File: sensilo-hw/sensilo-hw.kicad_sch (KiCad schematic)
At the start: 1 part

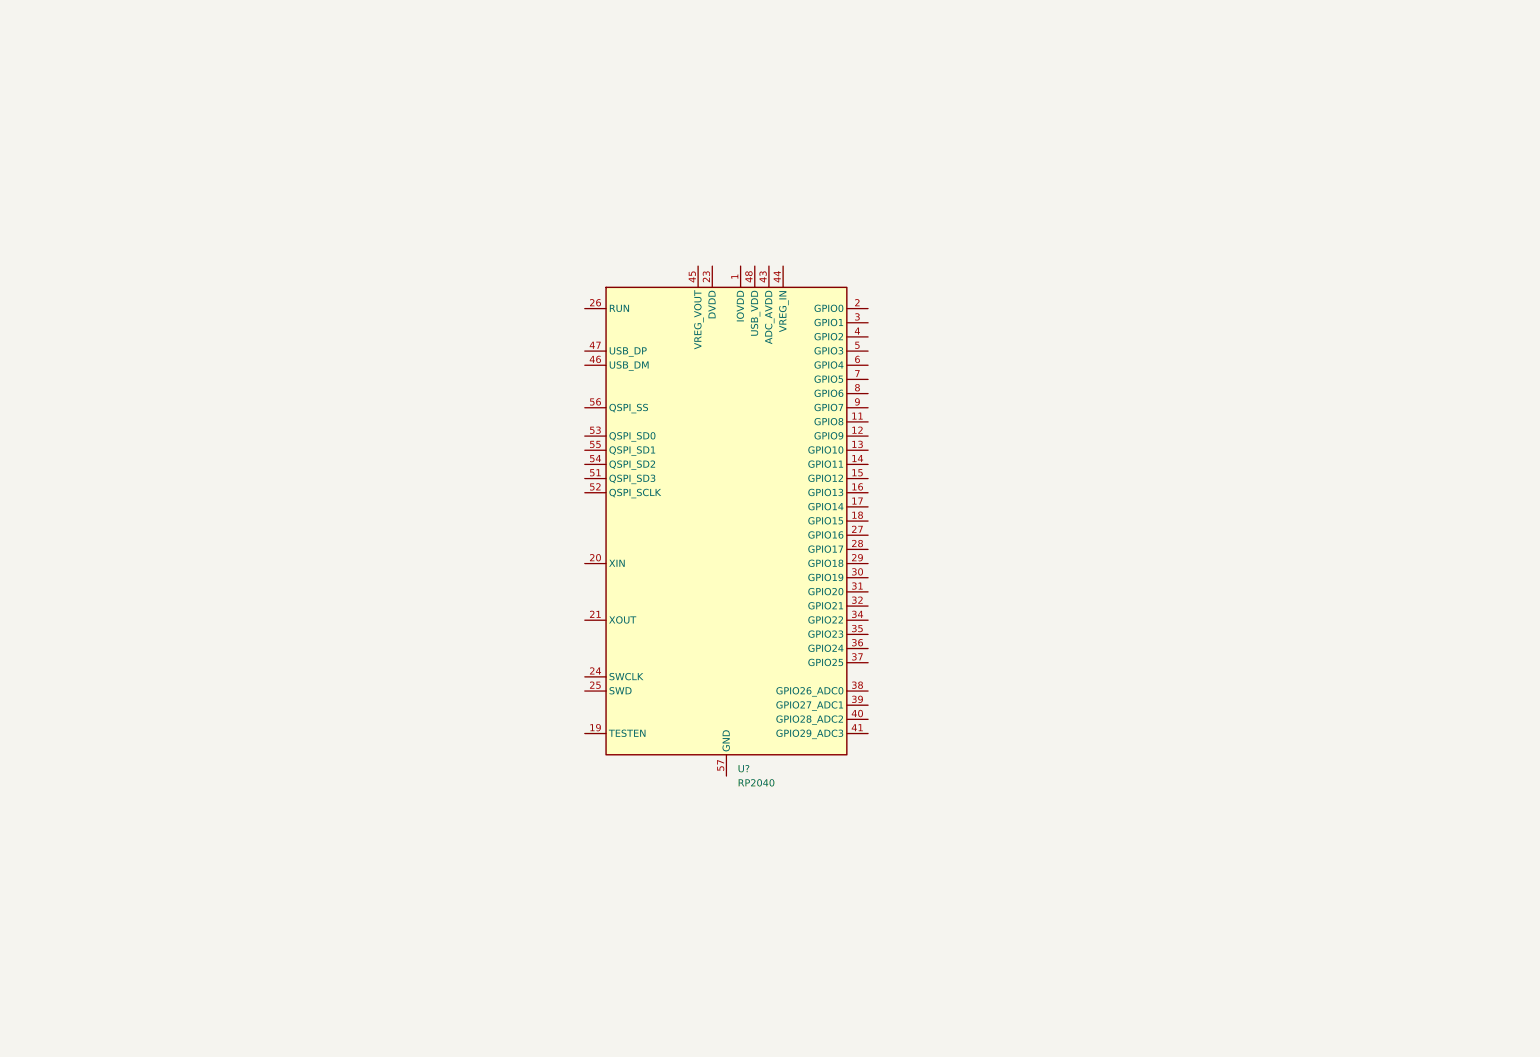
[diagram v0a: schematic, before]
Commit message: Schematic complete up to 40pc
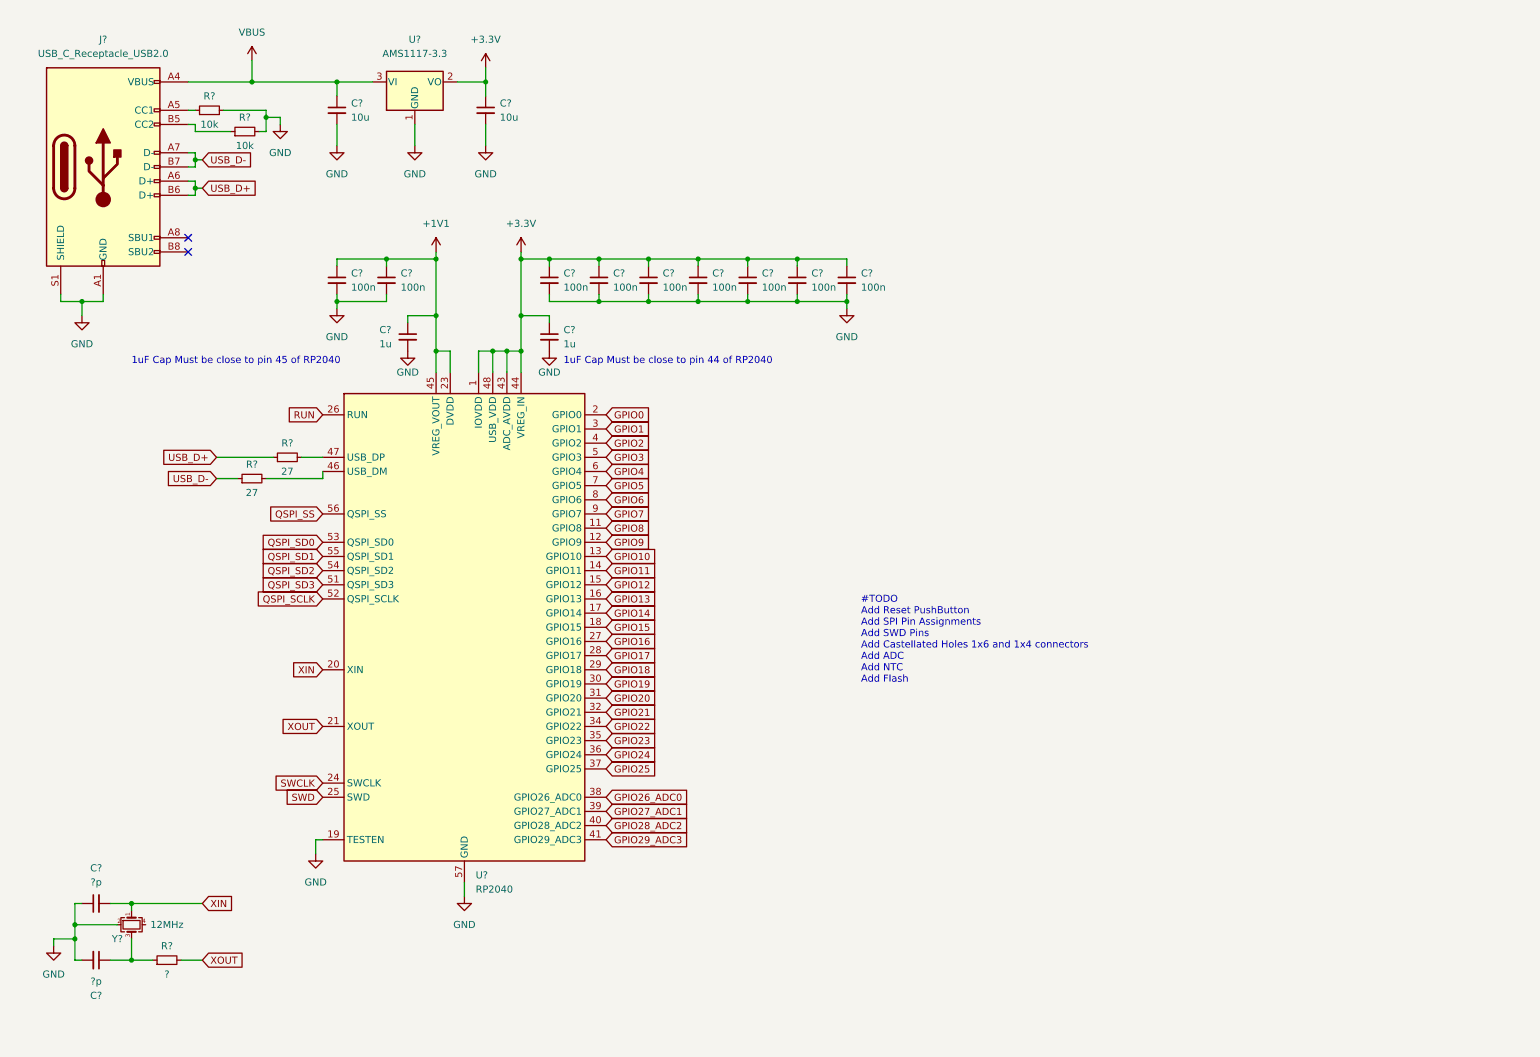
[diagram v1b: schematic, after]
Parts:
- added C? (x9): 100n, symbol Device:C_Small
- added C? (x2): 1u, symbol Device:C_Small
- added C? (x2): 10u, symbol Device:C_Small
- added C? (x2): ?p, symbol Device:C_Small
- added J?: USB_C_Receptacle_USB2.0, symbol Connector:USB_C_Receptacle_USB2.0
- added R? (x2): 10k, symbol Device:R_Small
- added R? (x2): 27, symbol Device:R_Small
- added R?: ?, symbol Device:R_Small
- added U?: AMS1117-3.3, Package_TO_SOT_SMD:SOT-223-3_TabPin2, symbol Regulator_Linear:AMS1117-3.3
- added Y?: 12MHz, Crystal:Crystal_SMD_3225-4Pin_3.2x2.5mm, symbol Device:Crystal_GND24_Small
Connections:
- net +3.3V: now reaches U?.1 (IOVDD), U?.10 (IOVDD), U?.22 (IOVDD), U?.33 (IOVDD), U?.42 (IOVDD), U?.49 (IOVDD)
- net +3.3V: now also U?.43 (ADC_AVDD), U?.44 (VREG_IN), U?.48 (USB_VDD), C?.1, C?.1, C?.1, C?.1, C?.1, C?.1, C?.1, C?.1, C?.1, U?.2 (VO)
- net GPIO8: now reaches U?.11 (GPIO8)
- net GPIO9: now reaches U?.12 (GPIO9)
- net GPIO10: now reaches U?.13 (GPIO10)
- net GPIO11: now reaches U?.14 (GPIO11)
- net GPIO12: now reaches U?.15 (GPIO12)
- net GPIO13: now reaches U?.16 (GPIO13)
- net GPIO14: now reaches U?.17 (GPIO14)
- net GPIO15: now reaches U?.18 (GPIO15)
- net GND: now reaches U?.19 (TESTEN)
- net GND: now also U?.57 (GND), C?.1, C?.2, C?.2, C?.2, C?.2, C?.2, C?.2, C?.2, C?.2, C?.2, C?.2, C?.2, C?.2, C?.2, C?.2, J?.A1 (GND), J?.A12 (GND), J?.B1 (GND), J?.B12 (GND), J?.S1 (SHIELD), R?.2, R?.2, U?.1 (GND), Y?.2
- net GPIO0: now reaches U?.2 (GPIO0)
- net XIN: now reaches U?.20 (XIN)
- net XIN: now also C?.2, Y?.1
- net XOUT: now reaches U?.21 (XOUT)
- net XOUT: now also R?.2
- net +1V1: now reaches U?.23 (DVDD), U?.50 (DVDD)
- net +1V1: now also U?.45 (VREG_VOUT), C?.1, C?.1, C?.1
- net SWCLK: now reaches U?.24 (SWCLK)
- net SWD: now reaches U?.25 (SWD)
- net RUN: now reaches U?.26 (RUN)
- net GPIO16: now reaches U?.27 (GPIO16)
- net GPIO17: now reaches U?.28 (GPIO17)
- net GPIO18: now reaches U?.29 (GPIO18)
- net GPIO1: now reaches U?.3 (GPIO1)
- net GPIO19: now reaches U?.30 (GPIO19)
- net GPIO20: now reaches U?.31 (GPIO20)
- net GPIO21: now reaches U?.32 (GPIO21)
- net GPIO22: now reaches U?.34 (GPIO22)
- net GPIO23: now reaches U?.35 (GPIO23)
- net GPIO24: now reaches U?.36 (GPIO24)
- net GPIO25: now reaches U?.37 (GPIO25)
- net GPIO26_ADC0: now reaches U?.38 (GPIO26_ADC0)
- net GPIO27_ADC1: now reaches U?.39 (GPIO27_ADC1)
- net GPIO2: now reaches U?.4 (GPIO2)
- net GPIO28_ADC2: now reaches U?.40 (GPIO28_ADC2)
- net GPIO29_ADC3: now reaches U?.41 (GPIO29_ADC3)
- net at U?.46 (USB_DM): now also R?.2
- net at U?.47 (USB_DP): now also R?.2
- net GPIO3: now reaches U?.5 (GPIO3)
- net QSPI_SD3: now reaches U?.51 (QSPI_SD3)
- net QSPI_SCLK: now reaches U?.52 (QSPI_SCLK)
- net QSPI_SD0: now reaches U?.53 (QSPI_SD0)
- net QSPI_SD2: now reaches U?.54 (QSPI_SD2)
- net QSPI_SD1: now reaches U?.55 (QSPI_SD1)
- net QSPI_SS: now reaches U?.56 (QSPI_SS)
- net GPIO4: now reaches U?.6 (GPIO4)
- net GPIO5: now reaches U?.7 (GPIO5)
- net GPIO6: now reaches U?.8 (GPIO6)
- net GPIO7: now reaches U?.9 (GPIO7)
- new net: J?.A5 (CC1), R?.1
- new net: J?.B5 (CC2), R?.1
- new net: C?.1, R?.1, Y?.3
- new net USB_D+: J?.A6 (D+), J?.B6 (D+), R?.1
- new net USB_D-: J?.A7 (D-), J?.B7 (D-), R?.1
- new net VBUS: C?.1, J?.A4 (VBUS), J?.A9 (VBUS), J?.B4 (VBUS), J?.B9 (VBUS), U?.3 (VI)
- no-connect marks 0 -> 2
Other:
- note added: "#TODO Add Reset PushButton Add SPI Pin Assignments Add SWD Pins Add Castellated Holes 1x6 and 1x4 connectors Add ADC Add NTC Add Flash"
- note added: "1uF Cap Must be close to pin 44 of RP2040"
- note added: "1uF Cap Must be close to pin 45 of RP2040"
- moved on the sheet: U?

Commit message: Schematic done 90pc, most footprint assignments done
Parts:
- added C16, C17, C19, C20, C21, C22, C23, C24: 100n, Capacitor_SMD:C_0402_1005Metric, symbol Device:C_Small
- added C18: 1u, Capacitor_SMD:C_0603_1608Metric, symbol Device:C_Small
- added C25, C26, C27, C28, C29, C30, C31, C32, C33, C34, C35, C36, C37, C38: 10n, Capacitor_SMD:C_0402_1005Metric, symbol Device:C_Small
- added J1, J2, J3, J4, J5, J6, J7, J8: Conn_01x06_Female, Connector_PinHeader_2.54mm_Extra:PinHeader_1x06_P2.54mm_Vertical_Castellated, symbol Connector:Conn_01x06_Female
- added L1: 39n, Inductor_SMD:L_0603_1608Metric, symbol Device:L_Small
- added Q1: ALS-PT19-315C, symbol Sensor_Optical:KPS-3227
- added R10, R11, R12, R13, R14, R15, R17, R6, R7, R8, R9: 1k, Resistor_SMD:R_0402_1005Metric, symbol Device:R_Small
- added R16: 5k, Resistor_SMD:R_0402_1005Metric, symbol Device:R_Small
- added R18: DNP, Resistor_SMD:R_0402_1005Metric, symbol Device:R_Small
- added R22: 0, Resistor_SMD:R_0603_1608Metric, symbol Device:R_Small
- added R23, R24, R25, R26, R27, R28: 27, Resistor_SMD:R_0402_1005Metric, symbol Device:R_Small
- added R29, R31: 0, Resistor_SMD:R_0402_1005Metric, symbol Device:R_Small
- added R3, R4: 5k1, Resistor_SMD:R_0402_1005Metric, symbol Device:R_Small
- added R30: 10k, symbol Device:R_Small
- added R5: 10k, Resistor_SMD:R_0402_1005Metric, symbol Device:R_Small
- added SW1: SW_SPST, symbol Switch:SW_SPST
- added SW2: SW_Push, symbol Switch:SW_Push
- added TH1: 10k, Resistor_SMD:R_0805_2012Metric, symbol Device:Thermistor_NTC
- added U2: W25Q128JVSIQ, Package_SO:SOIC-8_5.23x5.23mm_P1.27mm, symbol Memory_Flash:W25Q128JVS
- added U3: AD7124-8BBCPZ, Package_DFN_QFN:QFN-32-1EP_5x5mm_P0.5mm_EP3.6x3.6mm, symbol Analog_ADC_Extra:AD7124-8BBCPZ
- C1, C2: renamed from C?; value 10u -> 22u; footprint (none) -> Capacitor_SMD:C_0805_2012Metric
- C10, C11, C12, C13, C5, C6, C7, C8, C9: renamed from C?; footprint (none) -> Capacitor_SMD:C_0402_1005Metric
- C14, C15: renamed from C?; value ?p -> 30p; footprint (none) -> Capacitor_SMD:C_0402_1005Metric
- C3, C4: renamed from C?; footprint (none) -> Capacitor_SMD:C_0603_1608Metric
- J9: renamed from J?; footprint (none) -> Connector_USB:USB_C_Receptacle_Palconn_UTC16-G
- R1, R2: renamed from R?; value 10k -> 5k1; footprint (none) -> Resistor_SMD:R_0402_1005Metric
- R19, R20: renamed from R?; footprint (none) -> Resistor_SMD:R_0402_1005Metric
- R21: renamed from R?; value ? -> 1k; footprint (none) -> Resistor_SMD:R_0402_1005Metric
- gave numbers to parts that had none: 3
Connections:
- net +3.3V: now also C17.1, C20.1, J1.3 (Pin_3), J1.5 (Pin_5), J2.3 (Pin_3), J3.1 (Pin_1), L1.1, R18.2, R3.1, R4.1, R5.2, U2.8 (VCC), U3.2 (IOVDD)
- net GND: now also Y1.4, C16.2, C17.2, C19.2, C20.2, J1.2 (Pin_2), J1.4 (Pin_4), J2.2 (Pin_2), J2.6 (Pin_6), J3.4 (Pin_4), J4.6 (Pin_6), J8.1 (Pin_1), R22.1, R31.2, SW1.1 (A), SW2.1, U2.4 (GND), U3.3 (DGND)
- net GPIO10: now also J4.4 (Pin_4)
- net GPIO11: now also J4.5 (Pin_5)
- net GPIO14: now also J8.2 (Pin_2)
- net GPIO15: now also J8.3 (Pin_3)
- net GPIO16: now also J8.4 (Pin_4)
- net GPIO17: now also J8.5 (Pin_5)
- net GPIO18: now also J8.6 (Pin_6)
- net GPIO4: now also U3.27 (~{SYNC})
- net GPIO5: now also J3.5 (Pin_5)
- net GPIO6: now also J3.6 (Pin_6)
- net GPIO7: now also J4.1 (Pin_1)
- net GPIO8: now also J4.2 (Pin_2)
- net GPIO9: now also J4.3 (Pin_3)
- net QSPI_SCLK: now also U2.6 (CLK)
- net QSPI_SD0: now also U2.5 (DI(IO0))
- net QSPI_SD1: now also U2.2 (DO(IO1))
- net QSPI_SD2: now also U2.3 (IO2)
- net QSPI_SD3: now also U2.7 (IO3)
- net QSPI_SS: now also R17.2, R18.1, U2.1 (~{CS})
- net RUN: now also C16.1, R5.1, SW2.2
- net SWCLK: now also R25.1
- net SWD: now also R26.1
- net VBUS: now also J1.1 (Pin_1)
- net USB_RP-: now reaches R19.2, U1.46 (USB_DM)
- net USB_RP+: now reaches R20.2, U1.47 (USB_DP)
- net CC1: now reaches J9.A5 (CC1), R1.1
- net CC2: now reaches J9.B5 (CC2), R2.1
- net XTAL_OUT: now reaches C15.1, R21.1, Y1.3
- net GPIO0 renamed GPIO0_SPI0_RX
- net GPIO0_SPI0_RX: now also U3.28 (DOUT/~{RDY})
- net GPIO1 renamed GPIO1_SPI0_CSn
- net GPIO1_SPI0_CSn: now also U3.32 (~{CS})
- net GPIO12 renamed GPIO12_I2C0_SDA
- net GPIO12_I2C0_SDA: now also R28.1, R4.2
- net GPIO13 renamed GPIO13_I2C0_SCL
- net GPIO13_I2C0_SCL: now also R27.1, R3.2
- net GPIO19: no longer names the net of U1.30 (GPIO19)
- net GPIO2 renamed GPIO2_SPI0_SCK
- net GPIO2_SPI0_SCK: now also U3.30 (SCLK)
- net GPIO20 renamed GPIO20_UART1_TX
- net GPIO20_UART1_TX: now also R24.1
- net GPIO21 renamed GPIO21_UART1_RX
- net GPIO21_UART1_RX: now also R23.1
- net GPIO22: no longer names the net of U1.34 (GPIO22)
- net GPIO23: no longer names the net of U1.35 (GPIO23)
- net GPIO24: no longer names the net of U1.36 (GPIO24)
- net GPIO25: no longer names the net of U1.37 (GPIO25)
- net GPIO26_ADC0: no longer names the net of U1.38 (GPIO26_ADC0)
- net GPIO27_ADC1: no longer names the net of U1.39 (GPIO27_ADC1)
- net GPIO28_ADC2: no longer names the net of U1.40 (GPIO28_ADC2)
- net GPIO29_ADC3: no longer names the net of U1.41 (GPIO29_ADC3)
- net GPIO3 renamed GPIO3_SPI0_TX
- net GPIO3_SPI0_TX: now also U3.29 (DIN)
- new net: R14.1, R29.2, TH1.1
- new net: R31.1, U3.31 (CLK)
- new net: R15.1, R30.2, TH1.2
- new net +3.3VADC: C18.1, C21.1, L1.2, Q1.1, Q1.3, U3.26 (AVDD)
- new net AIN0_NTC+: C35.1, R14.2, U3.4 (AIN0)
- new net AIN10: C29.1, C33.1, R10.2, U3.16 (AIN10)
- new net AIN10_CN: J6.5 (Pin_5), R10.1
- new net AIN11: C30.1, C33.2, R11.2, U3.17 (AIN11)
- new net AIN11_CN: J6.6 (Pin_6), R11.1
- new net AIN12: C34.1, C37.1, R12.2, U3.18 (AIN12)
- new net AIN12_CONN: J7.2 (Pin_2), R12.1
- new net AIN13: C34.2, C38.1, R13.2, U3.19 (AIN13)
- new net AIN13_CONN: J7.3 (Pin_3), R13.1
- new net AIN1_NTC-: C36.1, R15.2, U3.5 (AIN1)
- new net AIN2_ALS: C24.1, Q1.2, Q1.4, R16.2, U3.6 (AIN2)
- new net AIN3_IEXC0: J5.1 (Pin_1), U3.7 (AIN3)
- new net AIN4_IEXC1: J5.3 (Pin_3), U3.8 (AIN4)
- new net AIN6: C25.1, C31.1, R6.2, U3.10 (AIN6)
- new net AIN6_CN: J5.5 (Pin_5), R6.1
- new net AIN7: C26.1, C31.2, R7.2, U3.11 (AIN7)
- new net AIN7_CN: J5.6 (Pin_6), R7.1
- new net AIN8: C27.1, C32.1, R8.2, U3.14 (AIN8)
- new net AIN8_CN: J6.2 (Pin_2), R8.1
- new net AIN9: C28.1, C32.2, R9.2, U3.15 (AIN9)
- new net AIN9_CN: J6.3 (Pin_3), R9.1
- new net GNDA: C18.2, C21.2, C22.2, C23.2, C24.2, C25.2, C26.2, C27.2, C28.2, C29.2, C30.2, C35.2, C36.2, C37.2, C38.2, J5.2 (Pin_2), J5.4 (Pin_4), J6.1 (Pin_1), J6.4 (Pin_4), J7.1 (Pin_1), J7.4 (Pin_4), R16.1, R22.2, R30.1, U3.23 (AVSS), U3.25 (PSW), U3.33 (PAD)
- new net I2C_SCL: J3.2 (Pin_2), R27.2
- new net I2C_SDA: J3.3 (Pin_3), R28.2
- new net REFIN1M: J7.6 (Pin_6), U3.13 (REFIN1M)
- new net REFIN1P: J7.5 (Pin_5), U3.12 (REFIN1P)
- new net REFOUT: C23.1, R29.1, U3.22 (REFOUT)
- new net REGCAPA: C22.1, U3.24 (REGCAPA)
- new net REGCAPD: C19.1, U3.1 (REGCAPD)
- new net SWCLK_CN: J2.4 (Pin_4), R25.2
- new net SWD_CN: J2.5 (Pin_5), R26.2
- new net UART_RX: J1.6 (Pin_6), R23.2
- new net UART_TX: J2.1 (Pin_1), R24.2
- new net ~{USB_BOOT}: R17.1, SW1.2 (B)
- no-connect marks 2 -> 14
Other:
- note added: "AD7124 High Res ADC"
- note added: "AVDD Supply Filtering for ADC"
- note added: "Ain10-11 RC Filters"
- note added: "Ain12-13 RC Filters"
- note added: "Ain6-7 RC Filters"
- note added: "Ain8-9 RC Filters"
- note added: "Ambient Light Sensor"
- note added: "External Xtal"
- note added: "NTC Thermistor"
- note added: "Pull-up option in case CSb internal weak pull-up in RP2040 is not strong enough"
- note added: "QSPI Flash 128MB"
- note added: "RP2040 Xtal Flash"
- note added: "Reset Pushbutton"
- note added: "USB Connector and Power"
- note added: "Used for onboard sensors"
- moved on the sheet: C10, C11, C12, C13, C14, C15, C3, C4, C5, C6, C7, C8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
